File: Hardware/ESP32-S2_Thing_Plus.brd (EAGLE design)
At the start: 22.9 x 64.8 mm, 140 parts, among them J3 QWIIC_RA, J5 USB-C, J6 JTAG, Q1 2.5A/30V, Q2 MBT3904DW1T1, U1 ESP32-S2-WROOM, U2 CP210X, U3 AP2112K-3.3V, U4 MCP73831, U5 TC7USB40MU, Y1 32.768kHz

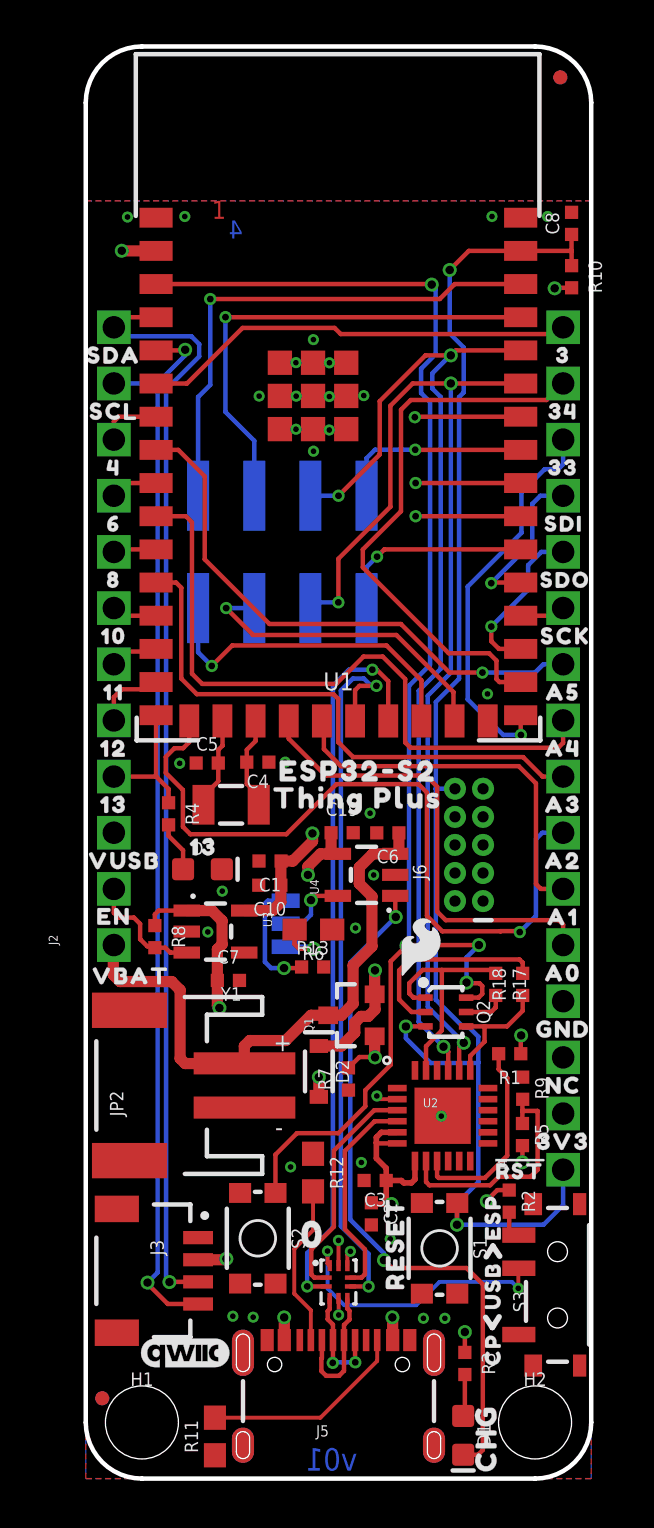
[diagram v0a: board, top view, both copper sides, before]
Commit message: added JTAG test points
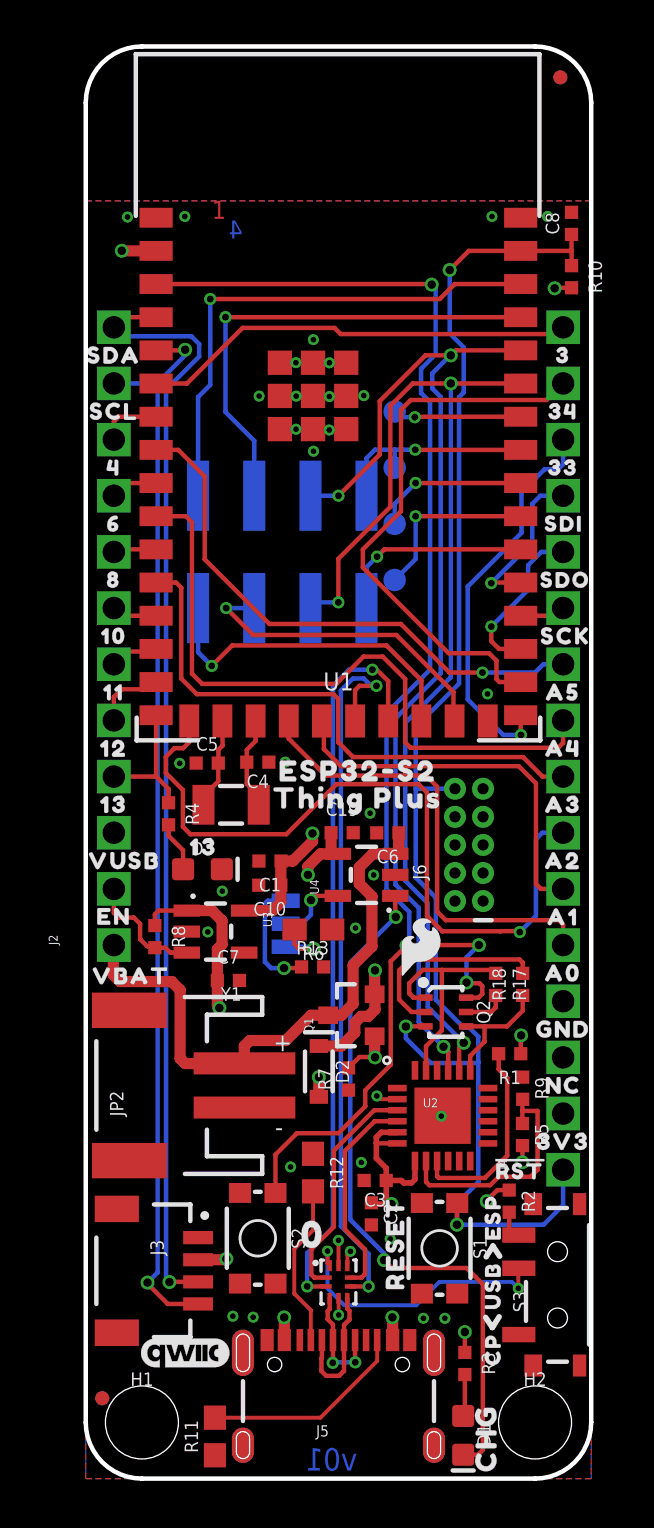
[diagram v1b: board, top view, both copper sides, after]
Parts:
- added TP2, TP3, TP4, TP5: (no value), SparkFun-Connectors:PAD.03X.04
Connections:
- net 41/MTDI: now also TP2.P$1
- net MTCK: now also TP4.P$1
- net MTDO: now also TP3.P$1
- net MTMS: now also TP5.P$1
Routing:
- net MTCK: track 21.6 -> 24.9 mm
- net MTDO: track 21.9 -> 24.1 mm
- net CHIP_PU: track 66.4 -> 68.1 mm
- net MTMS: track 28.0 -> 29.0 mm
- net RX0: track 47.5 -> 48.3 mm
- net 0: track 65.2 -> 66.1 mm
- net TX0: track 49.8 -> 50.7 mm
- net 41/MTDI: track 26.2 -> 27.0 mm

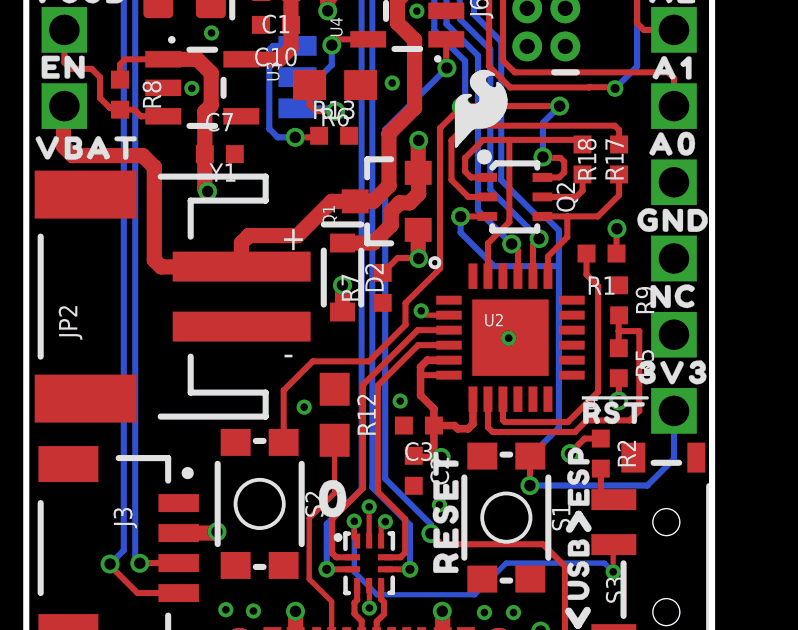
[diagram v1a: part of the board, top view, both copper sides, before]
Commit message: trestrict on cp210x and ground trace connection from outer pad to EPAD
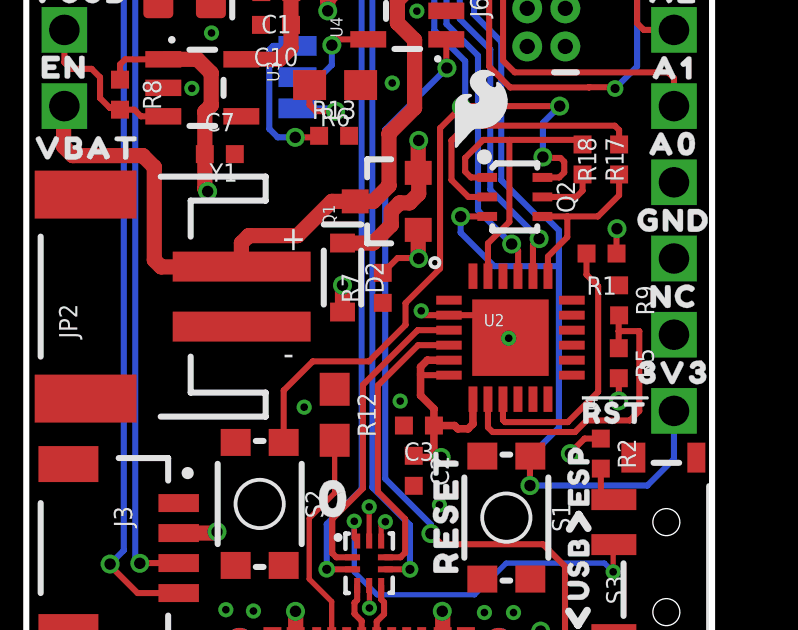
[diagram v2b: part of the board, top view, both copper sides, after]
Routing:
- net GND: track 2.38 -> 3.37 mm
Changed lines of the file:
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@@
 <layers>
 <layer number="1" name="Top" color="4" fill="1" visible="yes" active="yes"/>
-<layer number="2" name="Route2" color="1" fill="3" visible="yes" active="yes"/>
-<layer number="15" name="Route15" color="4" fill="6" visible="yes" active="yes"/>
-<layer number="16" name="Bottom" color="1" fill="1" visible="yes" active="yes"/>
+<layer number="2" name="Route2" color="1" fill="3" visible="no" active="yes"/>
+<layer number="15" name="Route15" color="4" fill="6" visible="no" active="yes"/>
+<layer number="16" name="Bottom" color="1" fill="1" visible="no" active="yes"/>
 <layer number="17" name="Pads" color="2" fill="1" visible="yes" active="yes"/>
 <layer number="18" name="Vias" color="2" fill="1" visible="yes" active="yes"/>
 <layer number="19" name="Unrouted" color="6" fill="1" visible="yes" active="yes"/>
 <layer number="20" name="Dimension" color="24" fill="1" visible="yes" active="yes"/>
-<layer number="21" name="tPlace" color="16" fill="1" visible="no" active="yes"/>
-<layer number="22" name="bPlace" color="14" fill="1" visible="yes" active="yes"/>
+<layer number="21" name="tPlace" color="16" fill="1" visible="yes" active="yes"/>
+<layer number="22" name="bPlace" color="14" fill="1" visible="no" active="yes"/>
 <layer number="23" name="tOrigins" color="15" fill="1" visible="yes" active="yes"/>
 <layer number="24" name="bOrigins" color="15" fill="1" visible="yes" active="yes"/>
@@
 <layer number="39" name="tKeepout" color="4" fill="11" visible="no" active="yes"/>
 <layer number="40" name="bKeepout" color="1" fill="11" visible="no" active="yes"/>
-<layer number="41" name="tRestrict" color="4" fill="10" visible="no" active="yes"/>
+<layer number="41" name="tRestrict" color="4" fill="10" visible="yes" active="yes"/>
 <layer number="42" name="bRestrict" color="1" fill="10" visible="no" active="yes"/>
 <layer number="43" name="vRestrict" color="2" fill="10" visible="no" active="yes"/>
@@
 <wire x1="11.21780625" y1="23.9771875" x2="11.108746875" y2="23.824865625" width="0.2032" layer="22"/>
 <wire x1="11.108746875" y1="23.824865625" x2="10.4026875" y2="23.939021875" width="0.2032" layer="22" curve="-114.277589"/>
+<rectangle x1="17.49551875" y1="16.28648125" x2="17.561559375" y2="16.5481" layer="41"/>
+<rectangle x1="14.716759375" y1="16.29918125" x2="14.782796875" y2="16.5608" layer="41"/>
+<rectangle x1="16.09216875" y1="14.893290625" x2="16.15820625" y2="15.154909375" layer="41" rot="R90"/>
+<rectangle x1="16.07946875" y1="17.67713125" x2="16.14550625" y2="17.93875" layer="41" rot="R90"/>
 </plain>
 <attributes>
@@
 <wire x1="11.43" y1="8.15" x2="11.437625" y2="8.142375" width="0.1778" layer="1"/>
 <wire x1="11.437625" y1="8.142375" x2="11.437625" y2="7.399015625" width="0.1778" layer="1"/>
-<wire x1="14.0891625" y1="17.160940625" x2="13.175678125" y2="17.160940625" width="0.1778" layer="1"/>
 <wire x1="13.175678125" y1="17.160940625" x2="13.167359375" y2="17.152621875" width="0.1778" layer="1"/>
 <via x="16.080740625" y="16.3931625" extent="1-16" drill="0.254"/>
@@
 <via x="10.2997" y="46.464225" extent="1-16" drill="0.254"/>
 <contactref element="C8" pad="2"/>
+<wire x1="14.0891625" y1="17.160940625" x2="15.060359375" y2="17.160940625" width="0.2032" layer="1"/>
+<wire x1="15.060359375" y1="17.160940625" x2="15.072359375" y2="17.172940625" width="0.2032" layer="1"/>
+<wire x1="14.0891625" y1="17.160940625" x2="13.175678125" y2="17.160940625" width="0.2032" layer="1"/>
 </signal>
 <signal name="DTR">
